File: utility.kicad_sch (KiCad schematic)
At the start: 0 parts

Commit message: MCU migration completed
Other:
- title: (none) -> RBC by UGS
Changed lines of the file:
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@@
 (kicad_sch (version 20230121) (generator eeschema)
   (paper "A4")
+  (title_block
+    (title "RBC by UGS")
+    (date "2023-09-04")
+    (rev "2.0")
+  )
 )

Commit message: implemented battery level detection
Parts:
- added D1 (x4): Green, symbol Device:LED
- added D1: Red, symbol Device:LED
- added R27 (x5): 1k, symbol Device:R_Small
- added R33: 18k ±5%, symbol Device:R_Small
- added R37: 82k ±1%, symbol Device:R_Small
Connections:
- new net: D1.2 (A), R27.2 (x5)
- new net +BATT: R37.1
- new net 1_BATT_IND: R27.1
- new net 2_BATT_IND: R27.1
- new net 3_BATT_IND: R27.1
- new net 4_BATT_IND: R27.1
- new net 5_BATT_IND: R27.1
- new net BATT_LVL: R33.1, R37.2
- new net GND: D1.1 (K), D1.1 (K), D1.1 (K), D1.1 (K), D1.1 (K), R33.2
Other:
- note added: "6S battery step-down"
- note added: "~4.536 max"

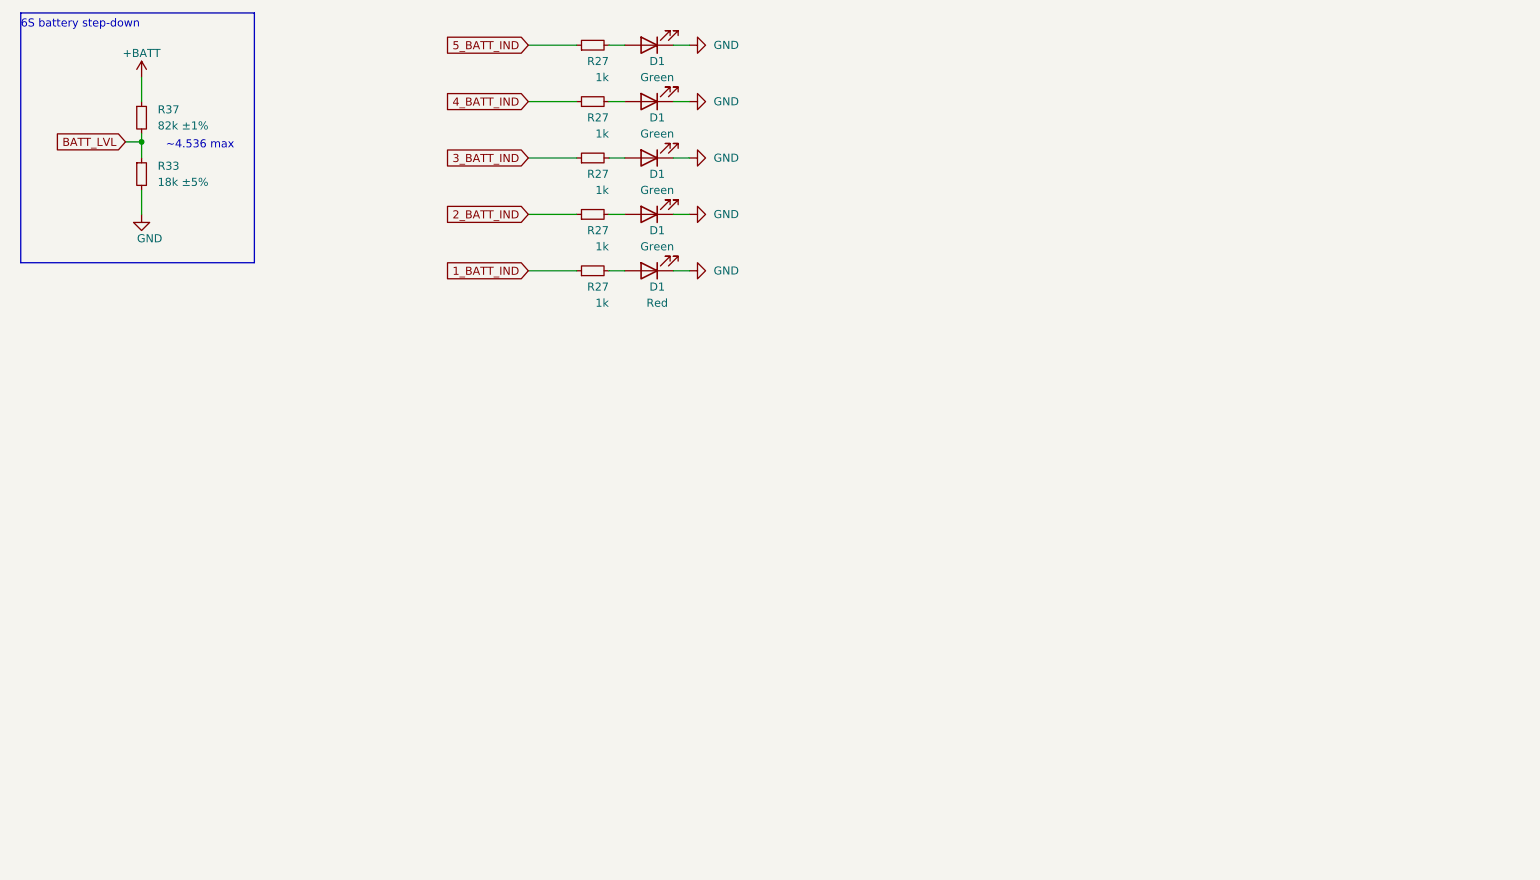
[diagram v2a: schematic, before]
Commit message: Completed full schematics
New features:
- extra 5V reg for handling camera current
- extra 12V reg for powering external LEDs
- added circuit for external emergency stop switch
- added some solder jumper for design flexibility
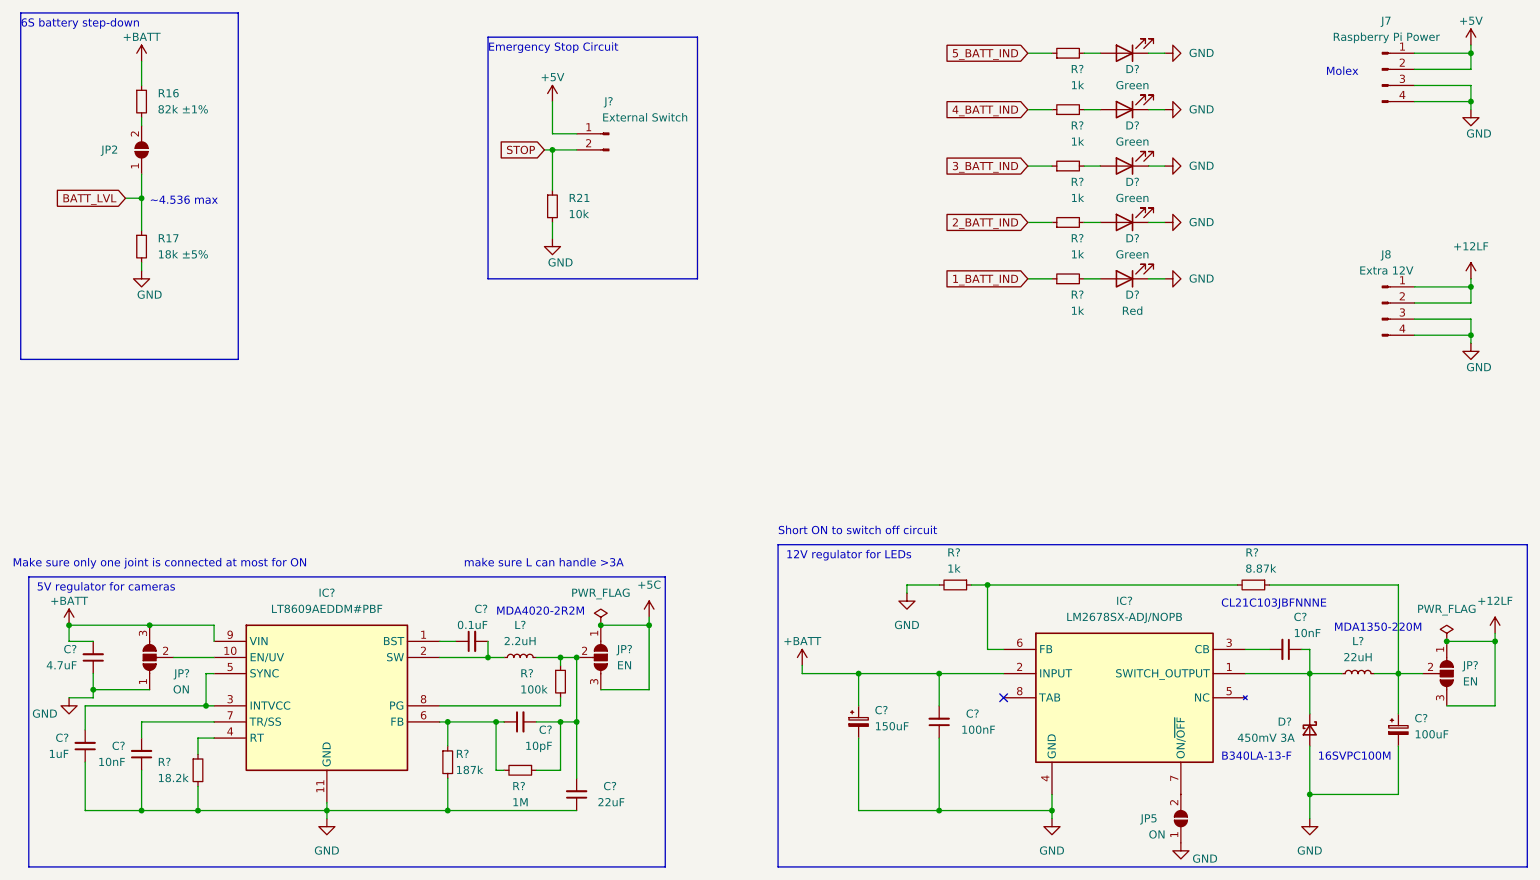
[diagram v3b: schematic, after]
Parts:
- added C?: 100uF, symbol Device:C_Polarized_Small
- added C?: 4.7uF, Capacitor_SMD:C_0603_1608Metric_Pad1.08x0.95mm_HandSolder, symbol Device:C_Small
- added C? (x2): 10nF, Capacitor_SMD:C_0603_1608Metric_Pad1.08x0.95mm_HandSolder, symbol Device:C_Small
- added C?: 150uF, symbol Device:C_Polarized_Small
- added C?: 10pF, Capacitor_SMD:C_0603_1608Metric_Pad1.08x0.95mm_HandSolder, symbol Device:C_Small
- added C?: 0.1uF, Capacitor_SMD:C_0603_1608Metric_Pad1.08x0.95mm_HandSolder, symbol Device:C_Small
- added C?: 22uF, Capacitor_SMD:C_0603_1608Metric_Pad1.08x0.95mm_HandSolder, symbol Device:C_Small
- added C?: 1uF, Capacitor_SMD:C_0603_1608Metric_Pad1.08x0.95mm_HandSolder, symbol Device:C_Small
- added C?: 100nF, Capacitor_SMD:C_0603_1608Metric_Pad1.08x0.95mm_HandSolder, symbol Device:C_Small
- added D?: 450mV 3A, symbol Device:D_Schottky_Small
- added IC?: LM2678SX-ADJ/NOPB, SamacSys_Parts:KTW0007B, symbol SamacSys_Parts:LM2678SX-5.0_NOPB
- added IC?: LT8609AEDDM#PBF, SamacSys_Parts:SON50P300X300X80-11N-D, symbol SamacSys_Parts:LT8609AEDDM#PBF
- added J7: Raspberry Pi Power, symbol Connector:Conn_01x04_Pin
- added J8: Extra 12V, symbol Connector:Conn_01x04_Pin
- added J?: External Switch, TerminalBlock_Phoenix:TerminalBlock_Phoenix_MKDS-3-2-5.08_1x02_P5.08mm_Horizontal, symbol Connector:Conn_01x02_Pin
- added JP2: SolderJumper_2_Open, symbol Jumper:SolderJumper_2_Open
- added JP5: ON, symbol Jumper:SolderJumper_2_Open
- added JP? (x2): EN, Jumper:SolderJumper-3_P2.0mm_Open_TrianglePad1.0x1.5mm, symbol Jumper:SolderJumper_3_Open
- added JP?: ON, Jumper:SolderJumper-3_P2.0mm_Open_TrianglePad1.0x1.5mm, symbol Jumper:SolderJumper_3_Open
- added L?: 2.2uH, LQH3NPH150MMEL:IND_LQH3NPH150MMEL, symbol Device:L_Small
- added L?: 22uH, LQH3NPH150MMEL:IND_LQH3NPH150MMEL, symbol Device:L_Small
- added R21: 10k, symbol Device:R_Small
- added R?: 8.87k, Resistor_SMD:R_0805_2012Metric_Pad1.20x1.40mm_HandSolder, symbol Device:R_Small
- added R?: 187k, Resistor_SMD:R_0805_2012Metric_Pad1.20x1.40mm_HandSolder, symbol Device:R_Small
- added R?: 1M, Resistor_SMD:R_0805_2012Metric_Pad1.20x1.40mm_HandSolder, symbol Device:R_Small
- added R?: 100k, Resistor_SMD:R_0805_2012Metric_Pad1.20x1.40mm_HandSolder, symbol Device:R_Small
- added R?: 1k, Resistor_SMD:R_0805_2012Metric_Pad1.20x1.40mm_HandSolder, symbol Device:R_Small
- added R?: 18.2k, Resistor_SMD:R_0805_2012Metric_Pad1.20x1.40mm_HandSolder, symbol Device:R_Small
- renumbered D1 to D?, R37 to R16, R33 to R17, R27 to R?
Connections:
- net +BATT: now also C?.1, C?.2, C?.2, IC?.2 (INPUT), IC?.9 (VIN), JP?.3 (B)
- net BATT_LVL: now also JP2.1 (A); no longer R16.2
- net GND: now also C?.1, C?.1, C?.1, C?.1, C?.1, C?.2, C?.2, D?.2 (A), IC?.11 (GND), IC?.4 (GND), J7.3 (Pin_3), J7.4 (Pin_4), J8.3 (Pin_3), J8.4 (Pin_4), JP5.1 (A), JP?.1 (A), R21.2, R?.2, R?.2, R?.2
- new net: C?.2, IC?.2 (SW), L?.1
- new net: C?.2, C?.2, JP?.2 (C), L?.2, R?.1, R?.1
- new net: C?.1, JP?.2 (C), L?.2, R?.1
- new net: C?.2, IC?.7 (TR/SS)
- new net: C?.1, D?.1 (K), IC?.1 (SWITCH_OUTPUT), L?.1
- new net: C?.2, IC?.3 (CB)
- new net: JP2.2 (B), R16.2
- new net: C?.1, IC?.6 (FB), R?.1, R?.2
- new net: IC?.7 (ON/~{OFF}), JP5.2 (B)
- new net: IC?.6 (FB), R?.1, R?.2
- new net: C?.1, IC?.1 (BST)
- new net: C?.2, IC?.3 (INTVCC), IC?.5 (SYNC)
- new net: IC?.8 (PG), R?.2
- new net: IC?.10 (EN/UV), JP?.2 (C)
- new net: IC?.4 (RT), R?.1
- new net +12LF: J8.1 (Pin_1), J8.2 (Pin_2), JP?.1 (A), JP?.3 (B)
- new net +5C: JP?.1 (A), JP?.3 (B)
- new net +5V: J7.1 (Pin_1), J7.2 (Pin_2), J?.1 (Pin_1)
- new net STOP: J?.2 (Pin_2), R21.1
- no-connect marks 0 -> 1
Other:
- note added: "12V regulator for LEDs"
- note added: "16SVPC100M"
- note added: "5V regulator for cameras"
- note added: "B340LA-13-F"
- note added: "CL21C103JBFNNNE"
- note added: "Emergency Stop Circuit"
- note added: "MDA1350-220M"
- note added: "MDA4020-2R2M"
- note added: "Make sure only one joint is connected at most for ON"
- note added: "Molex"
- note added: "Short ON to switch off circuit"
- note added: "make sure L can handle >3A"
- moved on the sheet: D?, R16, R17, R?

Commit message: finalised schematics
removed second 5V regulator
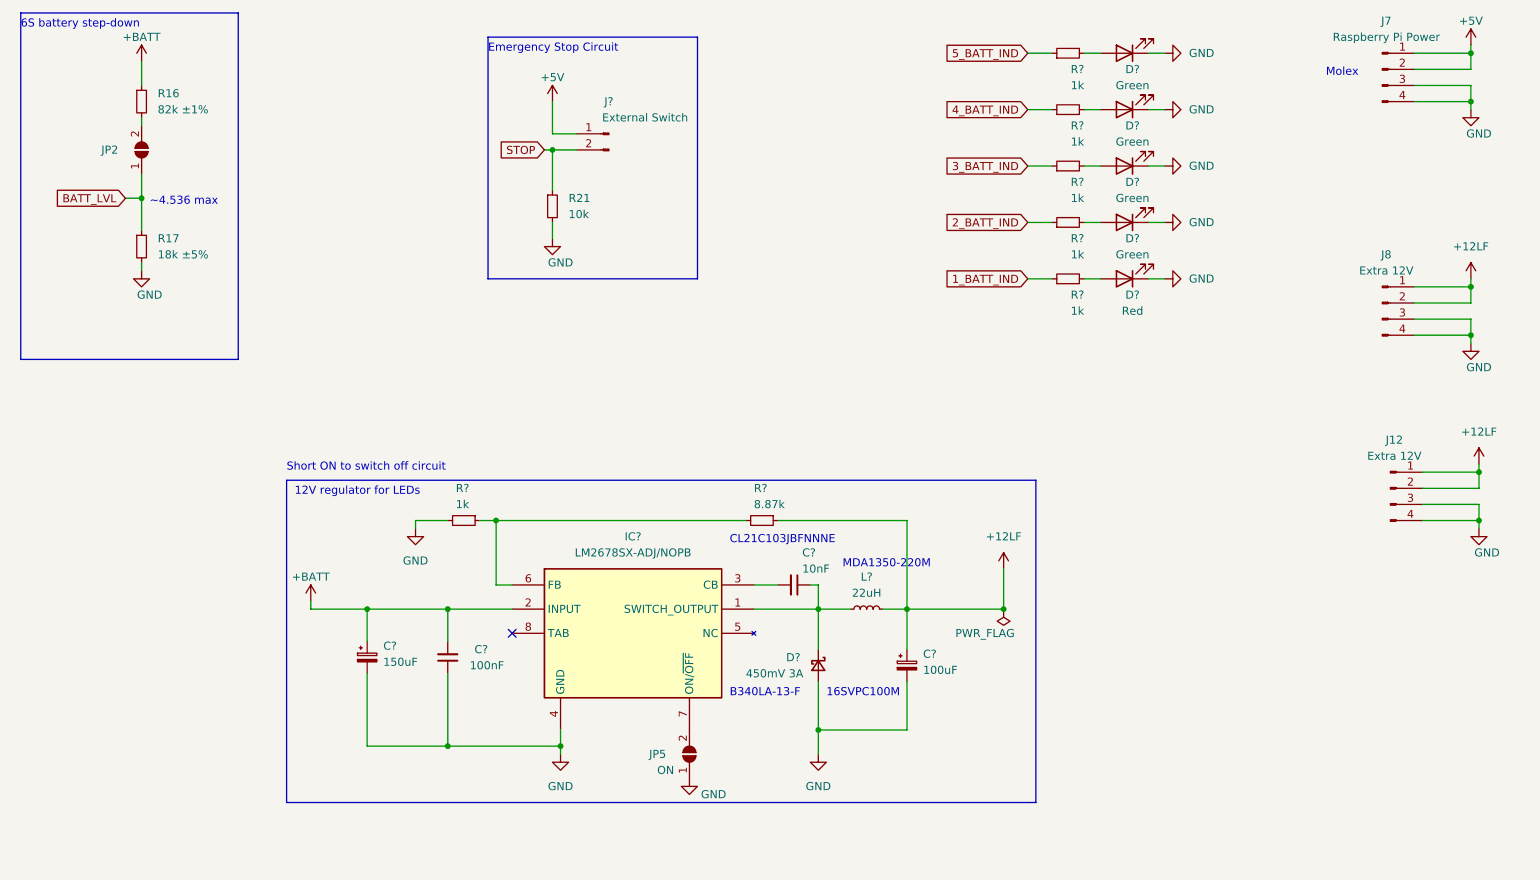
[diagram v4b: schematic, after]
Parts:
- removed C?: 4.7uF, Capacitor_SMD:C_0603_1608Metric_Pad1.08x0.95mm_HandSolder, symbol Device:C_Small
- removed C?: 10nF, Capacitor_SMD:C_0603_1608Metric_Pad1.08x0.95mm_HandSolder, symbol Device:C_Small
- removed C?: 10pF, Capacitor_SMD:C_0603_1608Metric_Pad1.08x0.95mm_HandSolder, symbol Device:C_Small
- removed C?: 0.1uF, Capacitor_SMD:C_0603_1608Metric_Pad1.08x0.95mm_HandSolder, symbol Device:C_Small
- removed C?: 22uF, Capacitor_SMD:C_0603_1608Metric_Pad1.08x0.95mm_HandSolder, symbol Device:C_Small
- removed C?: 1uF, Capacitor_SMD:C_0603_1608Metric_Pad1.08x0.95mm_HandSolder, symbol Device:C_Small
- removed IC?: LT8609AEDDM#PBF, SamacSys_Parts:SON50P300X300X80-11N-D, symbol SamacSys_Parts:LT8609AEDDM#PBF
- removed JP? (x2): EN, Jumper:SolderJumper-3_P2.0mm_Open_TrianglePad1.0x1.5mm, symbol Jumper:SolderJumper_3_Open
- removed JP?: ON, Jumper:SolderJumper-3_P2.0mm_Open_TrianglePad1.0x1.5mm, symbol Jumper:SolderJumper_3_Open
- removed L?: 2.2uH, LQH3NPH150MMEL:IND_LQH3NPH150MMEL, symbol Device:L_Small
- removed R?: 187k, Resistor_SMD:R_0805_2012Metric_Pad1.20x1.40mm_HandSolder, symbol Device:R_Small
- removed R?: 1M, Resistor_SMD:R_0805_2012Metric_Pad1.20x1.40mm_HandSolder, symbol Device:R_Small
- removed R?: 100k, Resistor_SMD:R_0805_2012Metric_Pad1.20x1.40mm_HandSolder, symbol Device:R_Small
- removed R?: 18.2k, Resistor_SMD:R_0805_2012Metric_Pad1.20x1.40mm_HandSolder, symbol Device:R_Small
- added J12: Extra 12V, symbol Connector:Conn_01x04_Pin
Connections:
- net +12LF: now also C?.1, L?.2, R?.1, J12.1 (Pin_1), J12.2 (Pin_2)
- net GND: now also J12.3 (Pin_3), J12.4 (Pin_4)
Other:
- note removed: "5V regulator for cameras"
- note removed: "MDA4020-2R2M"
- note removed: "Make sure only one joint is connected at most for ON"
- note removed: "make sure L can handle >3A"
- moved on the sheet: C?, D?, IC?, JP5, L?, R?

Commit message: footprint assignment WIP
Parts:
- renumbered J12 to J9, JP5 to JP3, R21 to R19

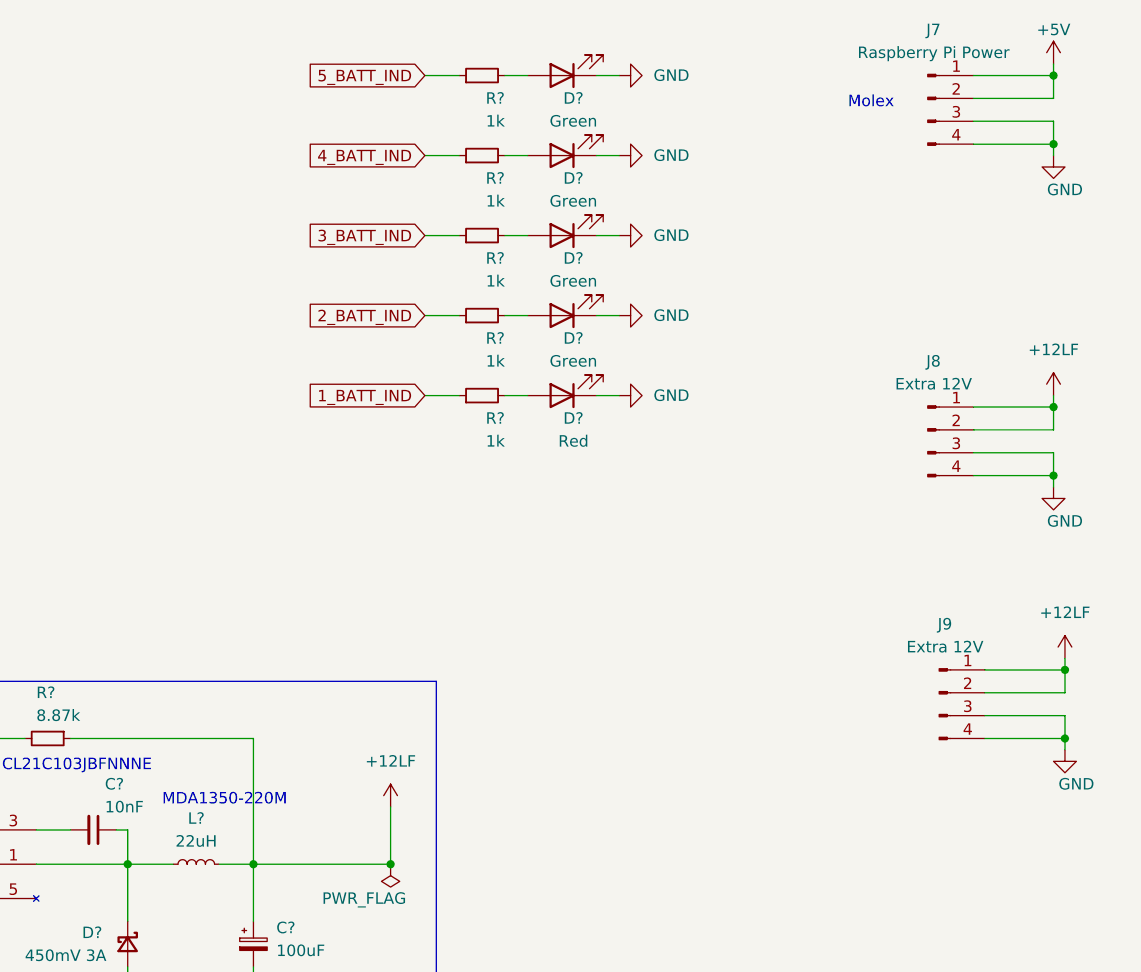
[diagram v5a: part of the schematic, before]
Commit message: completed footprint assignments
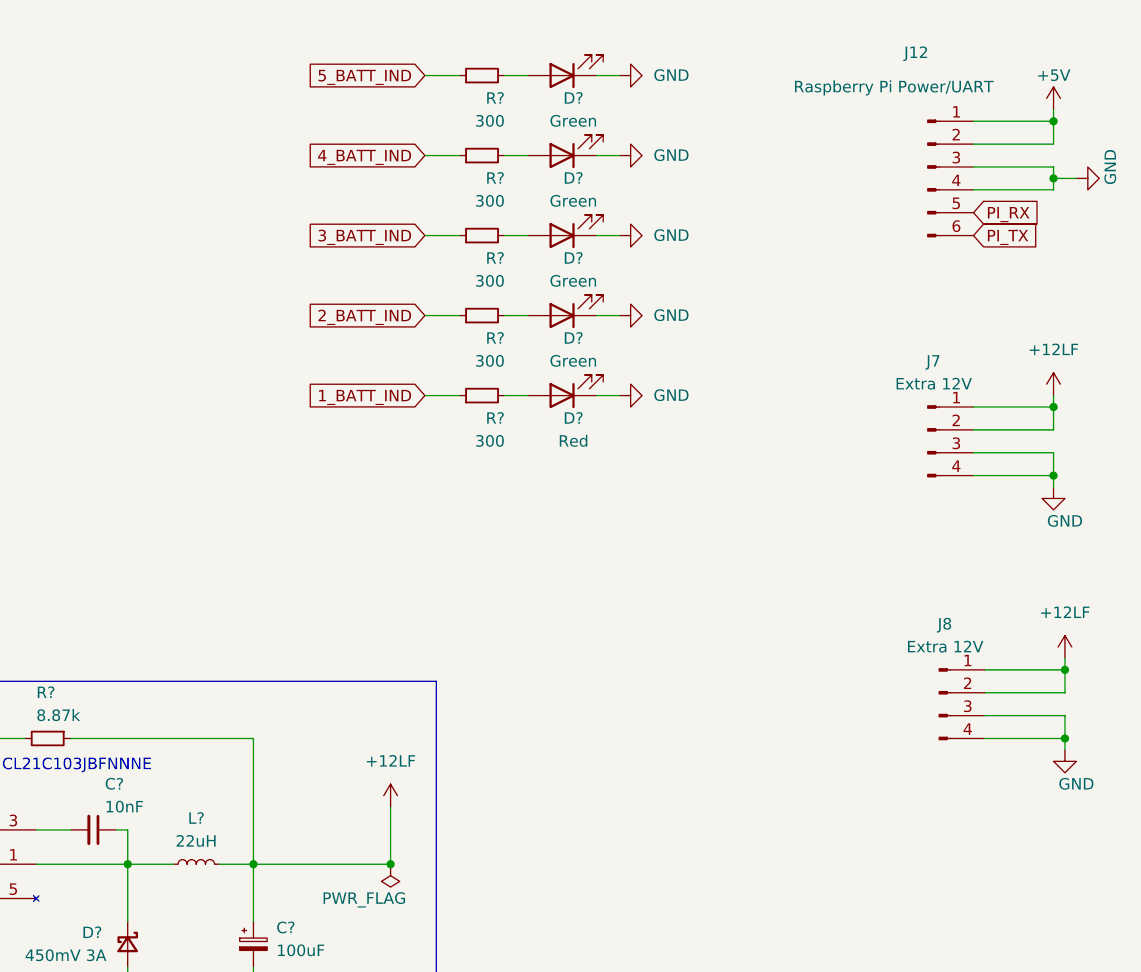
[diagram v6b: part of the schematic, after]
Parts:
- removed J7: Raspberry Pi Power, symbol Connector:Conn_01x04_Pin
- added J12: Raspberry Pi Power/UART, Connector_Molex:Molex_Micro-Fit_3.0_43045-0612_2x03_P3.00mm_Vertical, symbol Connector:Conn_01x06_Pin
- C?: footprint (none) -> SamacSys_Parts:16SVF180M
- C?: footprint Capacitor_SMD:C_0603_1608Metric_Pad1.08x0.95mm_HandSolder -> Capacitor_SMD:C_0805_2012Metric
- C?: footprint (none) -> SamacSys_Parts:EEHZT1E331UP
- C?: footprint Capacitor_SMD:C_0603_1608Metric_Pad1.08x0.95mm_HandSolder -> Capacitor_SMD:C_0402_1005Metric
- D?: footprint (none) -> Diode_SMD:D_SMA
- D? (x3): footprint (none) -> Diode_SMD:D_0805_2012Metric
- D?: footprint (none) -> Diode_SMD:D_0805_2012Metric; Part No. (none) -> 17-21/GHC-XS1T2M/3T
- D?: footprint (none) -> Diode_SMD:D_0805_2012Metric; Part No. (none) -> 17-215/R6C-AQ1R2B/3T
- J7: renamed from J8; footprint (none) -> Connector_Molex:Molex_Micro-Fit_3.0_43045-0412_2x02_P3.00mm_Vertical
- J8: renamed from J9; footprint (none) -> Connector_Molex:Molex_Micro-Fit_3.0_43045-0412_2x02_P3.00mm_Vertical
- JP2, JP3: footprint (none) -> Jumper:SolderJumper-2_P1.3mm_Open_RoundedPad1.0x1.5mm
- L?: footprint LQH3NPH150MMEL:IND_LQH3NPH150MMEL -> SamacSys_Parts:INDPM110100X400N
- R16: footprint (none) -> Resistor_SMD:R_0603_1608Metric_Pad0.98x0.95mm_HandSolder; Part No. (none) -> RTT038202FTP
- R17: footprint (none) -> Resistor_SMD:R_0603_1608Metric_Pad0.98x0.95mm_HandSolder
- R19: footprint (none) -> Resistor_SMD:R_0402_1005Metric
- R? (x5): value 1k -> 300; footprint (none) -> Resistor_SMD:R_0603_1608Metric_Pad0.98x0.95mm_HandSolder
- R?: footprint Resistor_SMD:R_0805_2012Metric_Pad1.20x1.40mm_HandSolder -> Resistor_SMD:R_0603_1608Metric
- R?: footprint Resistor_SMD:R_0805_2012Metric_Pad1.20x1.40mm_HandSolder -> Resistor_SMD:R_0201_0603Metric
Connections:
- net +5V: now also J12.1 (Pin_1), J12.2 (Pin_2)
- net GND: now also J12.3 (Pin_3), J12.4 (Pin_4)
- new net PI_RX: J12.5 (Pin_5)
- new net PI_TX: J12.6 (Pin_6)
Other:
- note removed: "MDA1350-220M"
- note removed: "Molex"
